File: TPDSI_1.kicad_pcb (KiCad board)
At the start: 2 copper layers, 83.8 x 61 mm, 64 parts, among them J1 Conn_01x02_Male, J2 Conn_01x02_Male, J3 Conn_01x10_Male, J4 Conn_01x04_Male, J5 Conn_01x04_Male, J6 Conn_01x06_Male, J7 Screw_Terminal_01x02, Q1 Q_NPN_BCE, Q2 Q_NPN_BCE, SW1 SW_Push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

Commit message: se comienza ruteo
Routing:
- net +3V3: track 31.1 -> 89.1 mm
- net /RB7: track 0.00 -> 32.1 mm, vias 0 -> 2
- net /RB6: track 0.00 -> 28.4 mm
- net /RD4: track 0.00 -> 23.8 mm
- net /RD5: track 0.00 -> 21.9 mm
- net /RD6: track 0.00 -> 20.8 mm
- net /RD7: track 0.00 -> 19.0 mm
- net /RB4: track 0.00 -> 17.5 mm
- net /RB5: track 0.00 -> 17.1 mm
- net /RB1: track 0.00 -> 16.2 mm
- net /RB2: track 0.00 -> 13.8 mm
- net /RB3: track 0.00 -> 12.1 mm
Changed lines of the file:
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@@
     (thickness 1.6)
     (drawings 17)
-    (tracks 13)
+    (tracks 89)
     (zones 0)
     (modules 64)
@@
   )
   (setup
-    (last_trace_width 1)
+    (last_trace_width 0.254)
     (user_trace_width 0.508)
     (user_trace_width 1)
@@
   (segment (start 178.233 107.055) (end 174.193 103.015) (width 1) (layer F.Cu) (net 4))
   (segment (start 180.333 107.055) (end 178.233 107.055) (width 1) (layer F.Cu) (net 4))
+  (segment (start 174.193 79.728) (end 171.803 79.728) (width 1) (layer B.Cu) (net 4))
+  (segment (start 123.262999 65.497999) (end 122.413 64.648) (width 1) (layer B.Cu) (net 4))
+  (segment (start 125.640201 67.875201) (end 123.262999 65.497999) (width 1) (layer B.Cu) (net 4))
+  (segment (start 159.950201 67.875201) (end 125.640201 67.875201) (width 1) (layer B.Cu) (net 4))
+  (segment (start 171.803 79.728) (end 159.950201 67.875201) (width 1) (layer B.Cu) (net 4))
   (segment (start 180.772999 68.397999) (end 179.273 66.898) (width 1) (layer F.Cu) (net 8))
   (segment (start 182.215999 68.397999) (end 180.772999 68.397999) (width 1) (layer F.Cu) (net 8))
   (segment (start 188.783 74.965) (end 182.215999 68.397999) (width 1) (layer F.Cu) (net 8))
   (segment (start 188.933 74.965) (end 188.783 74.965) (width 1) (layer F.Cu) (net 8))
+  (segment (start 128.622 71.912) (end 128.622 72.916) (width 0.254) (layer F.Cu) (net 16))
+  (segment (start 133.477 67.056) (end 128.622 71.912) (width 0.254) (layer F.Cu) (net 16))
+  (segment (start 138.9135 67.0315) (end 133.477 67.056) (width 0.254) (layer F.Cu) (net 16))
+  (segment (start 140.193 64.648) (end 140.193 65.752) (width 0.254) (layer F.Cu) (net 16))
+  (segment (start 140.193 65.752) (end 138.9135 67.0315) (width 0.254) (layer F.Cu) (net 16))
+  (segment (start 127.822 71.912) (end 127.822 72.916) (width 0.254) (layer F.Cu) (net 17))
+  (segment (start 133.223 66.421) (end 127.822 71.912) (width 0.254) (layer F.Cu) (net 17))
+  (segment (start 137.653 64.648) (end 135.509 66.421) (width 0.254) (layer F.Cu) (net 17))
+  (segment (start 135.509 66.421) (end 133.223 66.421) (width 0.254) (layer F.Cu) (net 17))
+  (segment (start 127.022 71.912) (end 127.022 72.916) (width 0.254) (layer F.Cu) (net 18))
+  (segment (start 133.108999 65.825001) (end 127.022 71.912) (width 0.254) (layer F.Cu) (net 18))
+  (segment (start 135.113 64.648) (end 133.935999 65.825001) (width 0.254) (layer F.Cu) (net 18))
+  (segment (start 133.935999 65.825001) (end 133.108999 65.825001) (width 0.254) (layer F.Cu) (net 18))
+  (segment (start 131.774962 64.648) (end 123.19 73.232962) (width 0.254) (layer F.Cu) (net 19))
+  (segment (start 132.573 64.648) (end 131.774962 64.648) (width 0.254) (layer F.Cu) (net 19))
+  (segment (start 124.318 76.216) (end 125.322 76.216) (width 0.254) (layer F.Cu) (net 19))
+  (segment (start 124.1124 76.216) (end 124.318 76.216) (width 0.254) (layer F.Cu) (net 19))
+  (segment (start 123.19 75.2936) (end 124.1124 76.216) (width 0.254) (layer F.Cu) (net 19))
+  (segment (start 123.19 73.232962) (end 123.19 75.2936) (width 0.254) (layer F.Cu) (net 19))
+  (segment (start 124.318 77.016) (end 125.322 77.016) (width 0.254) (layer F.Cu) (net 20))
+  (segment (start 124.270333 77.016) (end 124.318 77.016) (width 0.254) (layer F.Cu) (net 20))
+  (segment (start 122.73599 75.481657) (end 124.270333 77.016) (width 0.254) (layer F.Cu) (net 20))
+  (segment (start 122.73599 71.94501) (end 122.73599 75.481657) (width 0.254) (layer F.Cu) (net 20))
+  (segment (start 130.033 64.648) (end 122.73599 71.94501) (width 0.254) (layer F.Cu) (net 20))
+  (segment (start 116.521 77.816) (end 114.193 75.488) (width 0.254) (layer F.Cu) (net 21))
+  (segment (start 125.322 77.816) (end 124.298 77.816) (width 0.254) (layer F.Cu) (net 21))
+  (segment (start 121.666 75.946) (end 123.536 77.816) (width 0.254) (layer F.Cu) (net 21))
+  (segment (start 121.666 70.475) (end 121.666 75.946) (width 0.254) (layer F.Cu) (net 21))
+  (segment (start 127.493 64.648) (end 121.666 70.475) (width 0.254) (layer F.Cu) (net 21))
+  (segment (start 124.298 77.816) (end 123.536 77.816) (width 0.254) (layer F.Cu) (net 21))
+  (segment (start 123.536 77.816) (end 116.521 77.816) (width 0.254) (layer F.Cu) (net 21))
+  (segment (start 114.781 78.616) (end 114.193 78.028) (width 0.254) (layer F.Cu) (net 22))
+  (segment (start 125.322 78.616) (end 114.781 78.616) (width 0.254) (layer F.Cu) (net 22))
+  (segment (start 121.21199 68.38901) (end 121.21199 76.76199) (width 0.254) (layer F.Cu) (net 22))
+  (segment (start 124.953 64.648) (end 121.21199 68.38901) (width 0.254) (layer F.Cu) (net 22))
+  (via (at 121.412 76.962) (size 0.8) (drill 0.4) (layers F.Cu B.Cu) (net 22))
+  (segment (start 121.21199 76.76199) (end 121.412 76.962) (width 0.254) (layer F.Cu) (net 22))
+  (segment (start 121.412 76.962) (end 121.412 79.121) (width 0.254) (layer B.Cu) (net 22))
+  (via (at 121.412 79.502) (size 0.8) (drill 0.4) (layers F.Cu B.Cu) (net 22))
+  (segment (start 121.412 79.121) (end 121.412 79.502) (width 0.254) (layer B.Cu) (net 22))
+  (segment (start 122.298 78.616) (end 125.322 78.616) (width 0.254) (layer F.Cu) (net 22))
+  (segment (start 121.412 79.502) (end 122.298 78.616) (width 0.254) (layer F.Cu) (net 22))
+  (segment (start 144.2115 64.648) (end 145.3155 64.648) (width 0.254) (layer F.Cu) (net 27))
+  (segment (start 131.822 72.916) (end 131.822 69.353472) (width 0.254) (layer F.Cu) (net 27))
+  (segment (start 131.822 69.353472) (end 133.666312 67.50916) (width 0.254) (layer F.Cu) (net 27))
+  (segment (start 133.666312 67.50916) (end 138.914754 67.485509) (width 0.254) (layer F.Cu) (net 27))
+  (segment (start 142.72025 66.13925) (end 144.2115 64.648) (width 0.254) (layer F.Cu) (net 27))
+  (segment (start 138.914754 67.485509) (end 139.101557 67.485509) (width 0.254) (layer F.Cu) (net 27))
+  (segment (start 139.101557 67.485509) (end 140.447816 66.13925) (width 0.254) (layer F.Cu) (net 27))
+  (segment (start 140.447816 66.13925) (end 142.72025 66.13925) (width 0.254) (layer F.Cu) (net 27))
+  (segment (start 146.06625 66.43725) (end 147.8555 64.648) (width 0.254) (layer F.Cu) (net 28))
+  (segment (start 132.622 72.916) (end 132.622 69.195538) (width 0.254) (layer F.Cu) (net 28))
+  (segment (start 132.622 69.195538) (end 133.855216 67.962322) (width 0.254) (layer F.Cu) (net 28))
+  (segment (start 133.855216 67.962322) (end 138.915774 67.939519) (width 0.254) (layer F.Cu) (net 28))
+  (segment (start 145.91024 66.59326) (end 146.06625 66.43725) (width 0.254) (layer F.Cu) (net 28))
+  (segment (start 138.915774 67.939519) (end 139.289614 67.939518) (width 0.254) (layer F.Cu) (net 28))
+  (segment (start 139.289614 67.939518) (end 140.635872 66.59326) (width 0.254) (layer F.Cu) (net 28))
+  (segment (start 140.635872 66.59326) (end 145.91024 66.59326) (width 0.254) (layer F.Cu) (net 28))
+  (segment (start 133.422 72.916) (end 133.422 70.286) (width 0.254) (layer F.Cu) (net 29))
+  (segment (start 133.422 70.286) (end 135.298166 68.409834) (width 0.254) (layer F.Cu) (net 29))
+  (segment (start 139.461364 68.409834) (end 140.823928 67.04727) (width 0.254) (layer F.Cu) (net 29))
+  (segment (start 135.298166 68.409834) (end 139.461364 68.409834) (width 0.254) (layer F.Cu) (net 29))
+  (segment (start 147.99623 67.04727) (end 150.3955 64.648) (width 0.254) (layer F.Cu) (net 29))
+  (segment (start 140.823928 67.04727) (end 147.99623 67.04727) (width 0.254) (layer F.Cu) (net 29))
+  (segment (start 134.222 72.916) (end 134.222 70.128066) (width 0.254) (layer F.Cu) (net 30))
+  (segment (start 135.486222 68.863844) (end 139.851068 68.863844) (width 0.254) (layer F.Cu) (net 30))
+  (segment (start 134.222 70.128066) (end 135.486222 68.863844) (width 0.254) (layer F.Cu) (net 30))
+  (segment (start 152.085501 65.497999) (end 152.9355 64.648) (width 0.254) (layer F.Cu) (net 30))
+  (segment (start 150.08222 67.50128) (end 152.085501 65.497999) (width 0.254) (layer F.Cu) (net 30))
+  (segment (start 141.213632 67.50128) (end 150.08222 67.50128) (width 0.254) (layer F.Cu) (net 30))
+  (segment (start 139.851068 68.863844) (end 141.213632 67.50128) (width 0.254) (layer F.Cu) (net 30))
   (zone (net 1) (net_name GND) (layer F.Cu) (hatch edge 0.508)
     (connect_pads (clearance 0.4))

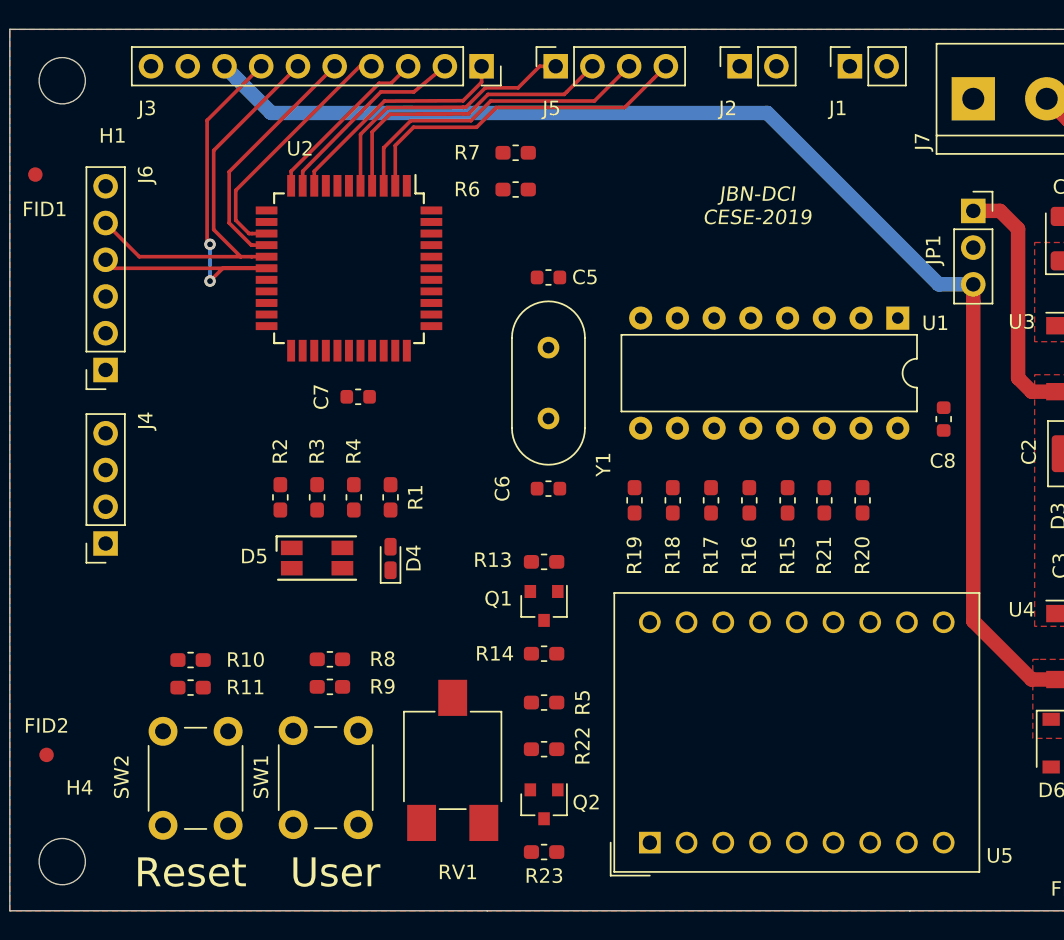
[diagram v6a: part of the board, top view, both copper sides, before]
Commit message: Se agregan ruteo de nuevas pistas
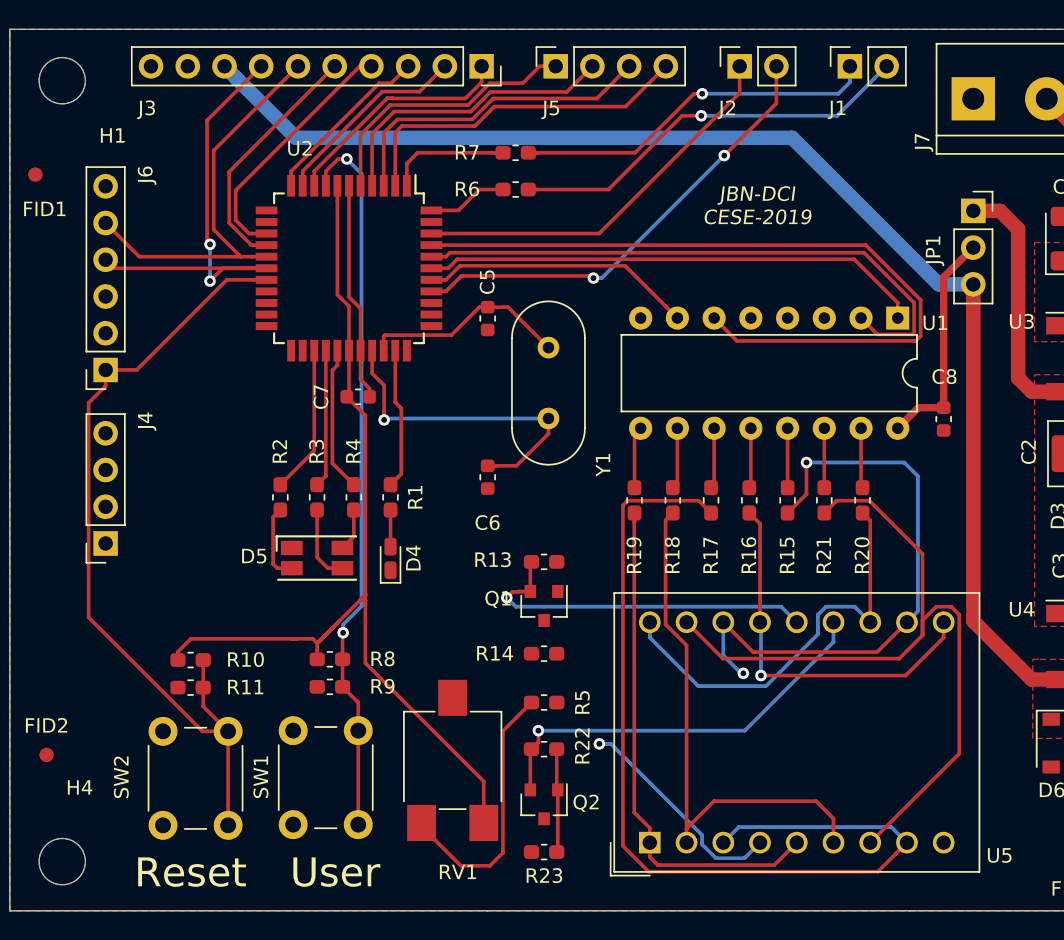
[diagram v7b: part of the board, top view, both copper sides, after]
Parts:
- moved C5 5.07 mm to (140.6, 82.1), turned to 90 degrees
- moved C6 4.28 mm to (140.6, 93.1), turned to 90 degrees
- turned C8 to 90 degrees
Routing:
- net VDD: track 0.00 -> 85.4 mm
- net /Display/c: track 0.00 -> 64.9 mm
- net /Microcontroller/MCLR_VPP: track 0.00 -> 56.4 mm
- net /Display/g: track 0.00 -> 54.8 mm
- net /Microcontroller/RD3: track 0.00 -> 53.0 mm
- net /Microcontroller/USER_BUTTON: track 0.00 -> 50.3 mm, vias 0 -> 2
- net /Microcontroller/RD2: track 0.00 -> 41.2 mm
- net /Display/a: track 0.00 -> 41.1 mm, vias 0 -> 2
- net /Display/d: track 0.00 -> 36.8 mm
- net /Display/e: track 0.00 -> 35.3 mm
- net /Microcontroller/RD1: track 0.00 -> 34.8 mm
- net /SDA: track 0.00 -> 32.2 mm, vias 0 -> 2
- net /Display/f: track 0.00 -> 29.0 mm
- net /Display/DIG2_CA: track 0.00 -> 28.6 mm, vias 0 -> 1
- net /Microcontroller/TX: track 0.00 -> 28.3 mm, vias 0 -> 1
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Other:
- net class analogica added: clearance 0.508, trace_width 0.254, via_dia 0.8, via_drill 0.4

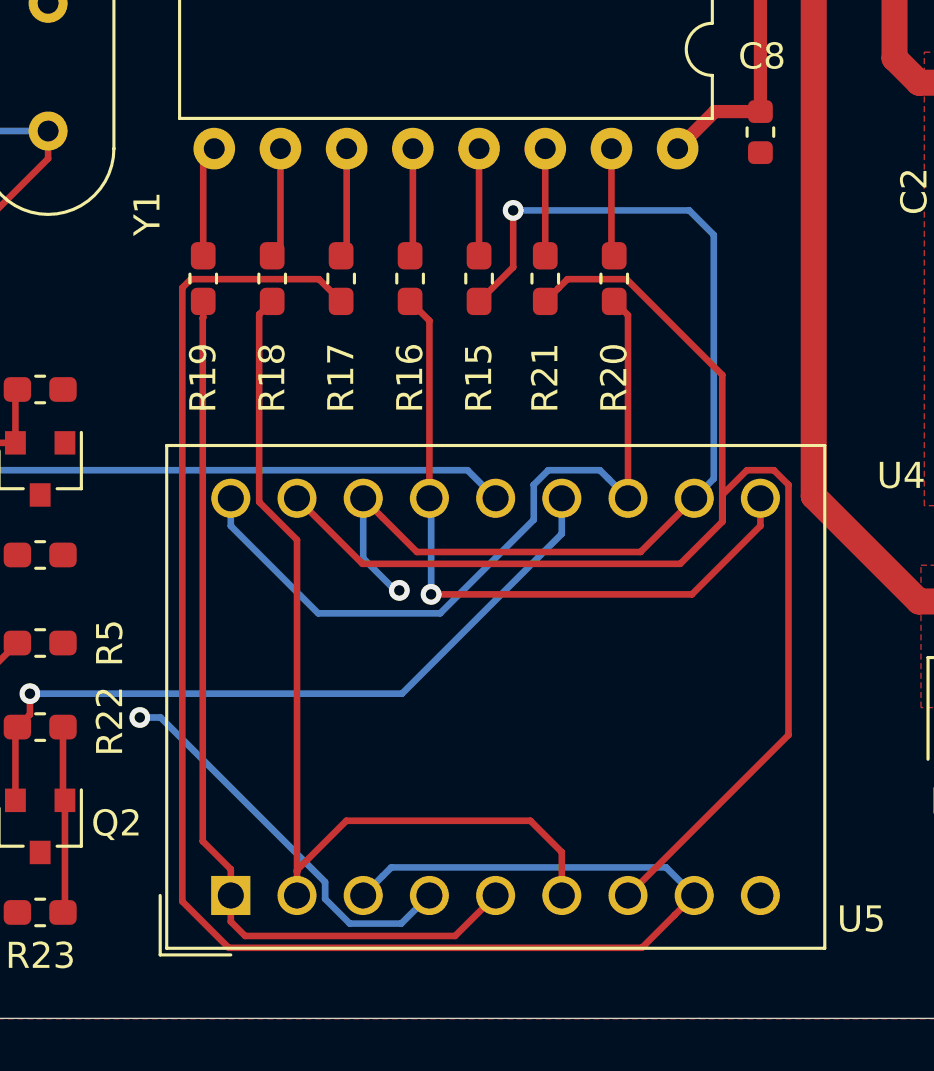
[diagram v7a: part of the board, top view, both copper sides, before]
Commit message: se modifican pistas display
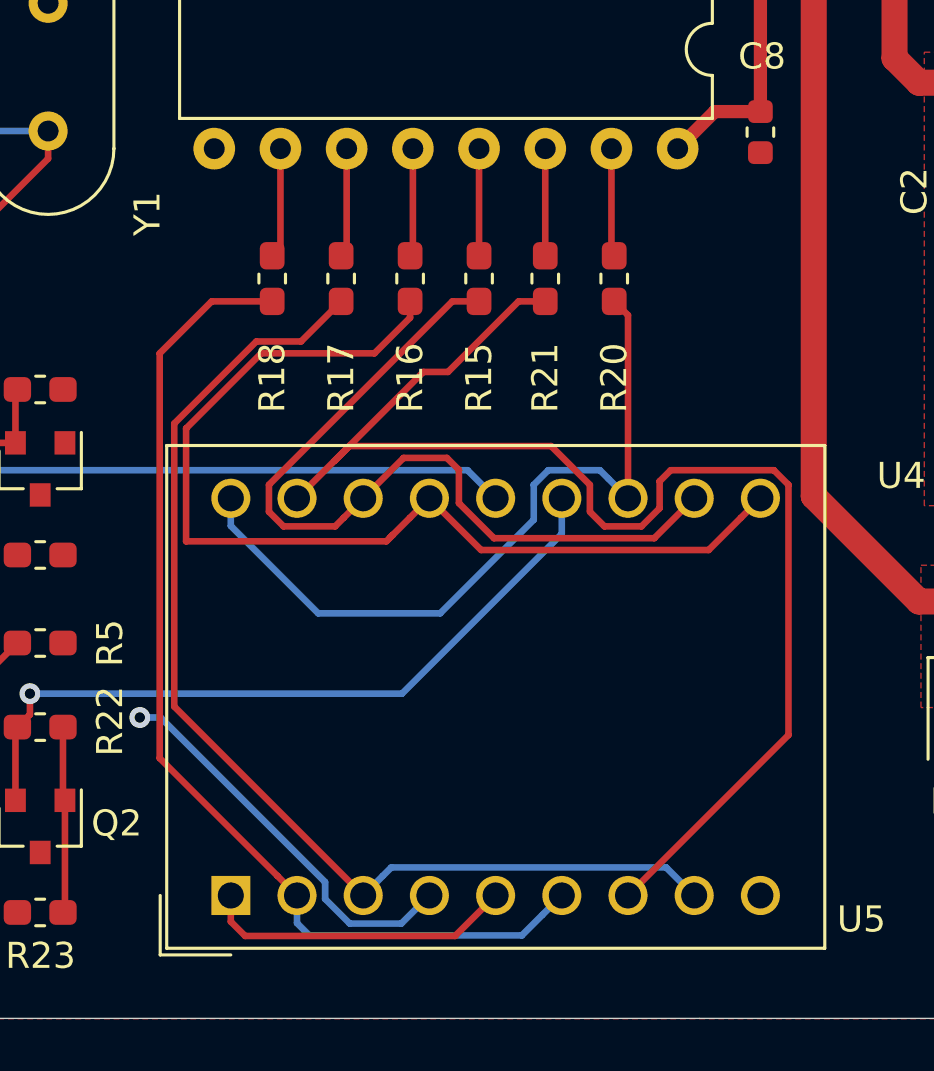
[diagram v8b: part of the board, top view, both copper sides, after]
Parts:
- removed R19: 330, Resistor_SMD:R_0603_1608Metric_Pad1.05x0.95mm_HandSolder
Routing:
- net /Display/e: track 35.3 -> 12.0 mm
- net /Display/c: track 64.9 -> 43.0 mm
- net /Display/b: track 26.4 -> 39.9 mm, vias 1 -> 0
- net /Display/a: track 41.1 -> 32.3 mm, vias 2 -> 0
- net Net-(R19-Pad2): track 4.29 -> 0.60 mm
- net /Display/d: track 36.8 -> 40.2 mm
- net /Display/g: track 54.8 -> 52.2 mm
